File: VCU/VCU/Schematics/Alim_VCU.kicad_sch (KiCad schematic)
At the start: 10 parts

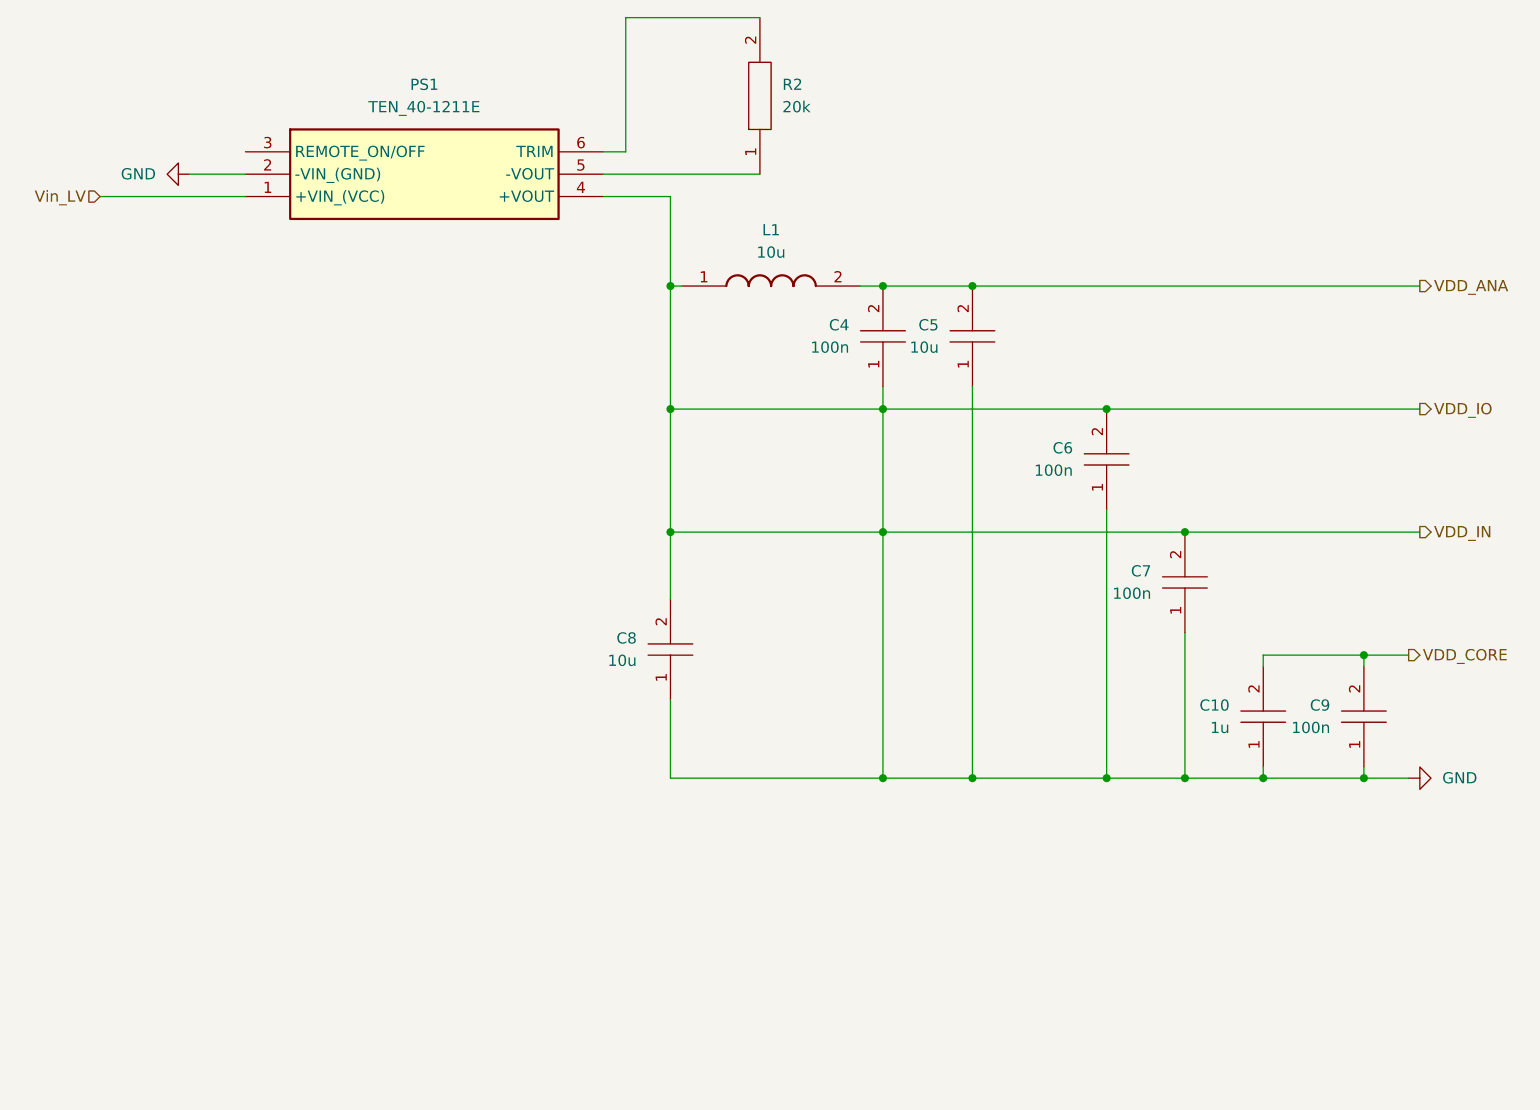
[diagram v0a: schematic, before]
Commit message: Update schematics
Update du schema avec ajout des embases et wiring de l'alimentation
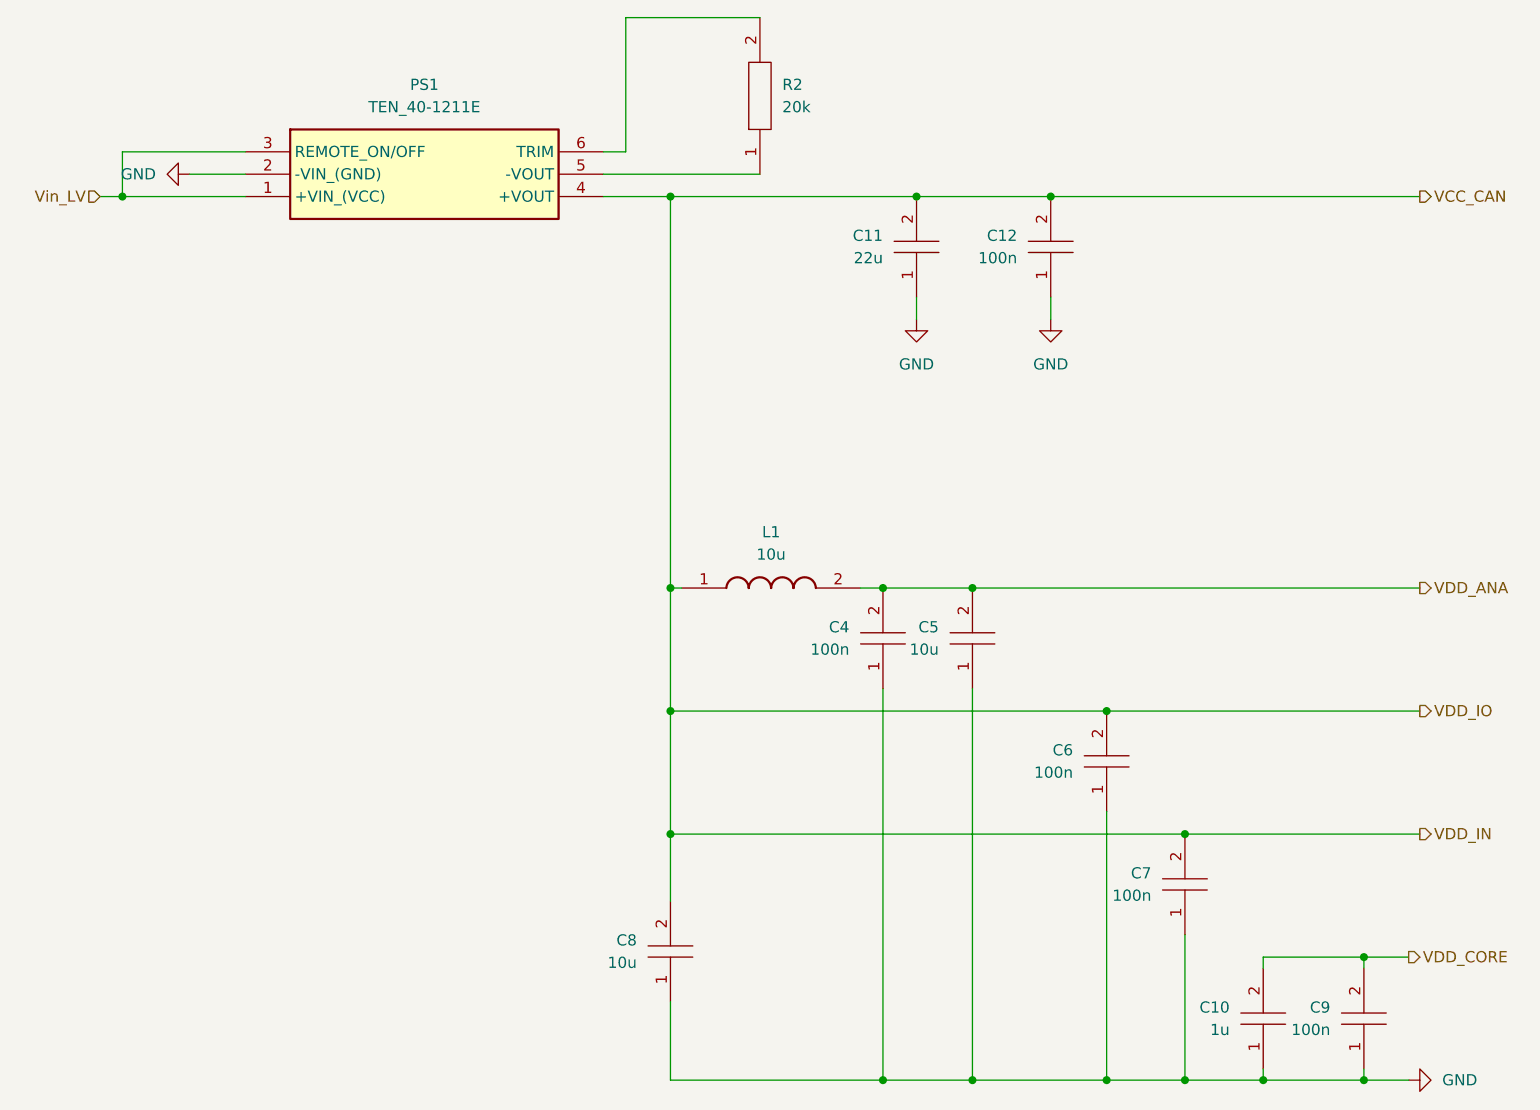
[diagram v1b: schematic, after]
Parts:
- added C11: 22u, EPSA_lib:CAPC2012X130N, symbol EPSA_lib:Condensateur 0805Y1000104JXT
- added C12: 100n, EPSA_lib:CAPC2012X130N, symbol EPSA_lib:Condensateur 0805Y1000104JXT
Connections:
- net GND: now also C11.1, C12.1; no longer C6.2, C7.2, C8.2, L1.1, PS1.4 (+VOUT)
- net Vin_LV: now also PS1.3 (REMOTE_ON/OFF)
- new net VCC_CAN: C11.2, C12.2, C6.2, C7.2, C8.2, L1.1, PS1.4 (+VOUT)
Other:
- moved on the sheet: C10, C4, C5, C6, C7, C8, C9, L1

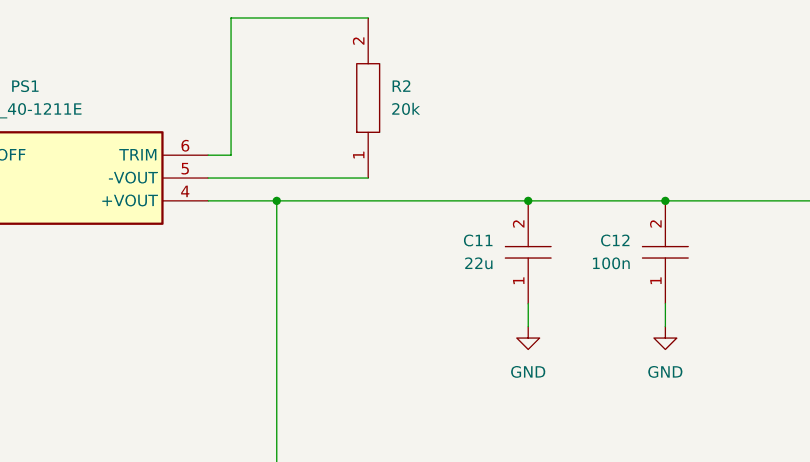
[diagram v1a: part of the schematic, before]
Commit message: Finalisation Schematics VCU Dev_Bench et tests codes
Finalisation des schematics pour le banc de test et de developpement du VCU, et ajout des premiers tests de code sur MPLAB effectués sur Dev board.
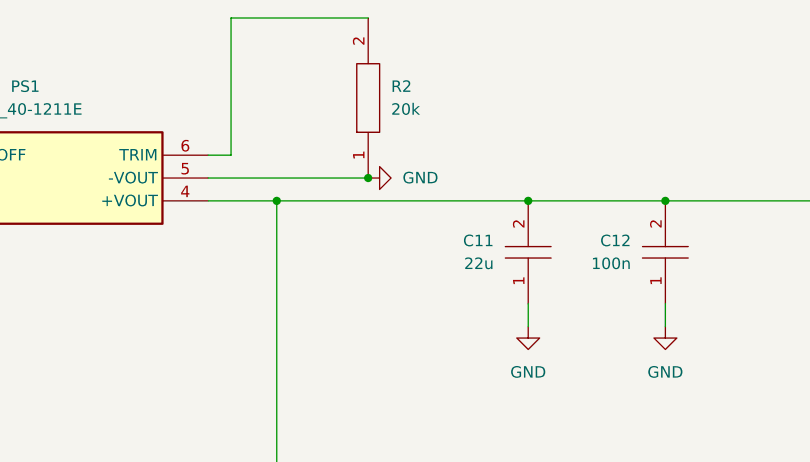
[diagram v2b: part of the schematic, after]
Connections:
- net GND: now also PS1.5 (-VOUT), R2.1
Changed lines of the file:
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@@
+	)
+	(junction
+		(at 120.65 44.45)
+		(diameter 0)
+		(color 0 0 0 0)
 	)
 	(junction
@@
 					(unit 1)
 				)
+			)
+		)
+	)
+	(symbol
+		(lib_id "power:GND")
+		(at 120.65 44.45 90)
+		(unit 1)
+		(exclude_from_sim no)
+		(in_bom yes)
+		(on_board yes)
+		(dnp no)
+		(fields_autoplaced yes)
+		(property "Reference" "#PWR018"
+			(at 127 44.45 0)
+			(effects
+				(font
+					(size 1.27 1.27)
+				)
+				(hide yes)
+			)
+		)
+		(property "Value" "GND"
+			(at 124.46 44.4499 90)
+			(effects
+				(font
+					(size 1.27 1.27)
+				)
+				(justify right)
+			)
+		)
+		(property "Footprint" ""
+			(at 120.65 44.45 0)
+			(effects
+				(font
+					(size 1.27 1.27)
+				)
+				(hide yes)
+			)
+		)
+		(property "Datasheet" ""
+			(at 120.65 44.45 0)
+			(effects
+				(font
+					(size 1.27 1.27)
+				)
+				(hide yes)
+			)
+		)
+		(property "Description" "Power symbol creates a global label with name \"GND\" , ground"
+			(at 120.65 44.45 0)
+			(effects
+				(font
+					(size 1.27 1.27)
+				)
+				(hide yes)
+			)
+		)
+		(pin "1"
+		)
+		(instances
+			(project "Schematics"
+				(path "/0ce89ae1-593d-4a2b-902e-7aca64ebde5a/ca07cadd-6105-492c-83f8-f0a02055fd2a"
+					(reference "#PWR018")
+					(unit 1)
+				)
